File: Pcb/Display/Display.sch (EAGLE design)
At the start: 31 parts, among them J2 47219-2001, Q1 310mA/60V/1.6Ω

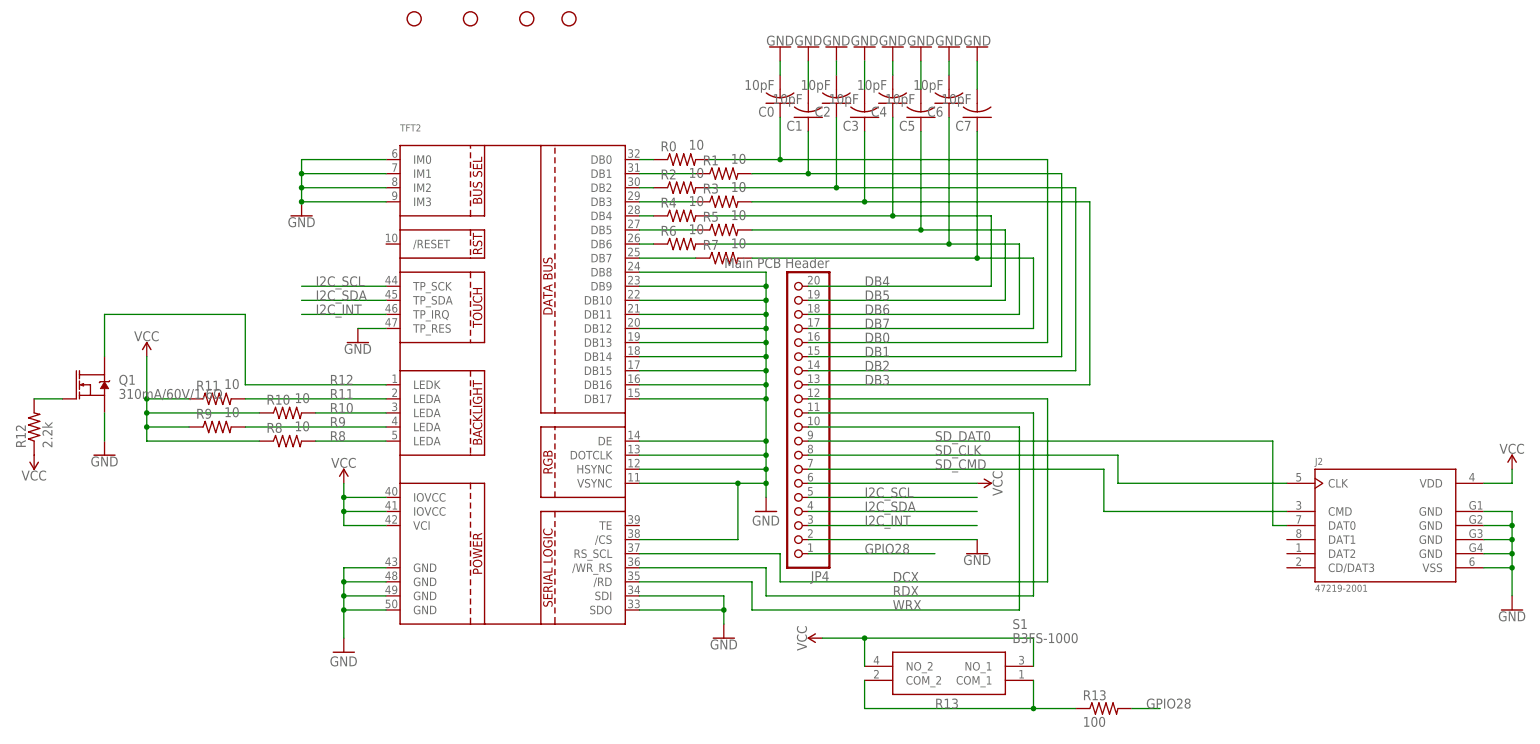
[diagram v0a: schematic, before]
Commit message: Updated PCB files and ported some of the graphics functions. The graphics changes are not tested yet.
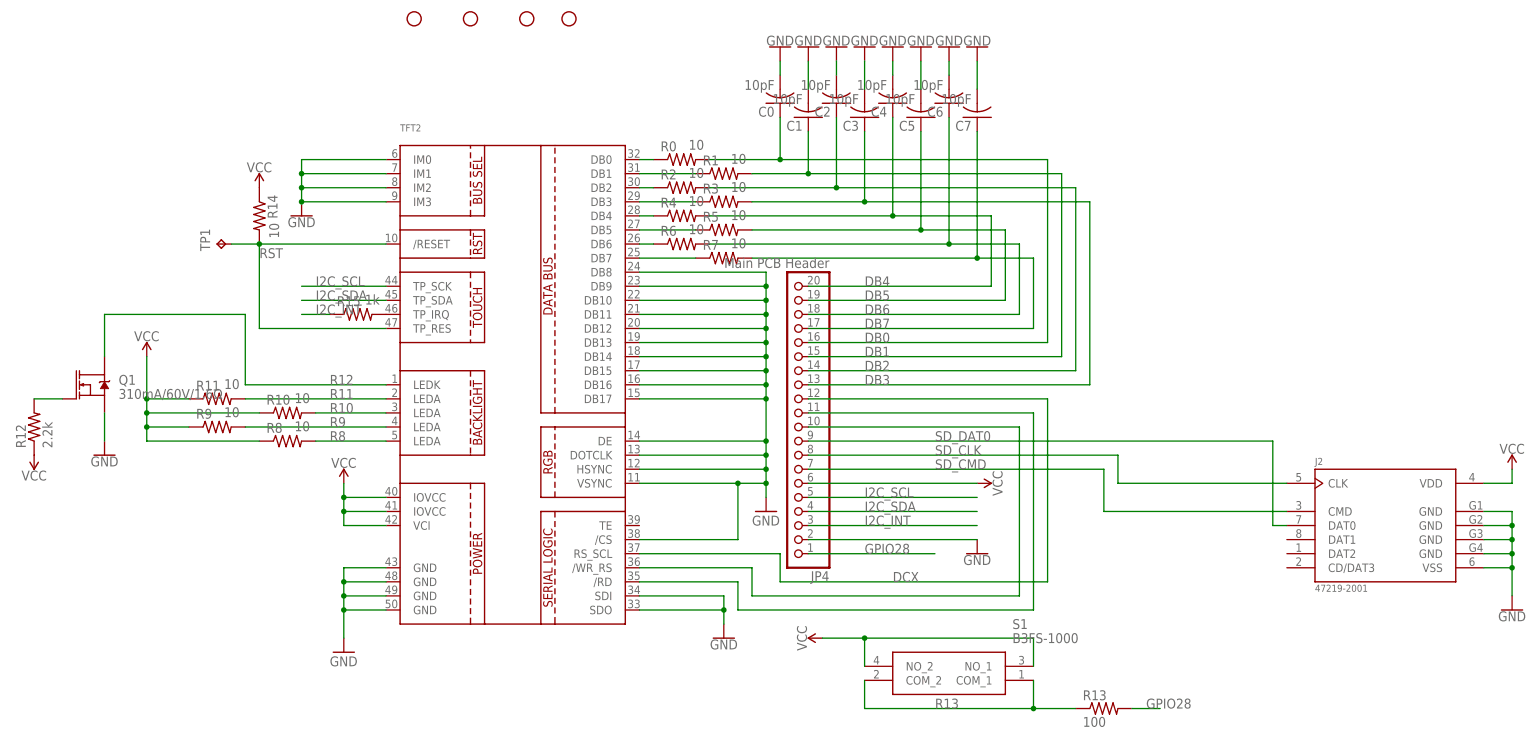
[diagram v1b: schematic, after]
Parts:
- added R14: 10, adafruit:R-US_R0805
- added R15: 1k, adafruit:R-US_R0805
- added TP1: TPTP09R, testpad:TPTP09R
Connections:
- new net N$4: R15.2, TFT2.TP_IRQ
- new net RST: R14.2, TFT2./RESET, TFT2.TP_RES, TP1.TP
- net GND: no longer TFT2.TP_RES
- net I2C_INT: now also R15.1; no longer TFT2.TP_IRQ
- net RDX: now also TFT2./RD; no longer TFT2./WR_RS
- net VCC: now also R14.1
- net WRX: now also TFT2./WR_RS; no longer TFT2./RD
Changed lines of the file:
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@@
 <?xml version="1.0" encoding="utf-8"?>
 <!DOCTYPE eagle SYSTEM "eagle.dtd">
-<eagle version="9.5.2">
+<eagle version="9.3.0">
 <drawing>
 <settings>
@@
 <part name="SUPPLY22" library="SparkFun-PowerSymbols" library_urn="urn:adsk.eagle:library:530" deviceset="VCC" device=""/>
 <part name="R12" library="rcl" library_urn="urn:adsk.eagle:library:334" deviceset="R-US_" device="M0805" package3d_urn="urn:adsk.eagle:package:23556/2" value="2.2k"/>
-<part name="GND40" library="SparkFun-PowerSymbols" library_urn="urn:adsk.eagle:library:530" deviceset="GND" device=""/>
 <part name="GND41" library="SparkFun-PowerSymbols" library_urn="urn:adsk.eagle:library:530" deviceset="GND" device=""/>
 <part name="R11" library="adafruit" deviceset="R-US_" device="R0805" value="10"/>
@@
 <part name="R6" library="adafruit" deviceset="R-US_" device="R0805" value="10"/>
 <part name="R7" library="adafruit" deviceset="R-US_" device="R0805" value="10"/>
+<part name="R14" library="adafruit" deviceset="R-US_" device="R0805" value="10"/>
+<part name="SUPPLY3" library="SparkFun-PowerSymbols" library_urn="urn:adsk.eagle:library:530" deviceset="VCC" device=""/>
+<part name="TP1" library="testpad" library_urn="urn:adsk.eagle:library:385" deviceset="TP" device="TP09R" package3d_urn="urn:adsk.eagle:package:27958/1"/>
+<part name="R15" library="adafruit" deviceset="R-US_" device="R0805" value="1k"/>
 </parts>
 <sheets>
@@
 <attribute name="VALUE" x="71.882" y="128.27" size="1.778" layer="96" rot="R90"/>
 </instance>
-<instance part="GND40" gate="1" x="127" y="147.32" smashed="yes">
-<attribute name="VALUE" x="127" y="147.066" size="1.778" layer="96" align="top-center"/>
-</instance>
 <instance part="GND41" gate="1" x="193.04" y="93.98" smashed="yes">
 <attribute name="VALUE" x="193.04" y="93.726" size="1.778" layer="96" align="top-center"/>
@@
 <attribute name="NAME" x="189.23" y="164.0586" size="1.778" layer="95"/>
 <attribute name="VALUE" x="194.31" y="164.338" size="1.778" layer="96"/>
+</instance>
+<instance part="R14" gate="G$1" x="109.22" y="170.18" smashed="yes" rot="R270">
+<attribute name="NAME" x="110.7186" y="173.99" size="1.778" layer="95" rot="R270"/>
+<attribute name="VALUE" x="110.998" y="168.91" size="1.778" layer="96" rot="R270"/>
+</instance>
+<instance part="SUPPLY3" gate="G$1" x="109.22" y="175.26" smashed="yes">
+<attribute name="VALUE" x="109.22" y="178.054" size="1.778" layer="96" align="bottom-center"/>
+</instance>
+<instance part="TP1" gate="G$1" x="101.6" y="165.1" smashed="yes" rot="R90">
+<attribute name="NAME" x="100.33" y="163.83" size="1.778" layer="95" rot="R90"/>
+<attribute name="TP_SIGNAL_NAME" x="102.87" y="166.37" size="1.778" layer="97" rot="R90"/>
+</instance>
+<instance part="R15" gate="G$1" x="127" y="152.4" smashed="yes">
+<attribute name="NAME" x="123.19" y="153.8986" size="1.778" layer="95"/>
+<attribute name="VALUE" x="128.27" y="154.178" size="1.778" layer="96"/>
 </instance>
 </instances>
@@
 </segment>
 <segment>
-<pinref part="TFT2" gate="G$1" pin="TP_RES"/>
-<wire x1="132.08" y1="149.86" x2="127" y2="149.86" width="0.1524" layer="91"/>
-<pinref part="GND40" gate="1" pin="GND"/>
-</segment>
-<segment>
 <pinref part="TFT2" gate="G$1" pin="SDI"/>
 <wire x1="177.8" y1="101.6" x2="193.04" y2="101.6" width="0.1524" layer="91"/>
@@
 <net name="I2C_INT" class="0">
 <segment>
-<pinref part="TFT2" gate="G$1" pin="TP_IRQ"/>
-<wire x1="132.08" y1="152.4" x2="116.84" y2="152.4" width="0.1524" layer="91"/>
-<label x="119.38" y="152.4" size="1.778" layer="95"/>
-</segment>
-<segment>
 <pinref part="JP4" gate="A" pin="3"/>
 <wire x1="208.28" y1="114.3" x2="238.76" y2="114.3" width="0.1524" layer="91"/>
 <label x="218.44" y="114.3" size="1.778" layer="95"/>
+</segment>
+<segment>
+<pinref part="R15" gate="G$1" pin="1"/>
+<wire x1="121.92" y1="152.4" x2="116.84" y2="152.4" width="0.1524" layer="91"/>
+<label x="119.38" y="152.4" size="1.778" layer="95"/>
 </segment>
 </net>
@@
 <pinref part="SUPPLY2" gate="G$1" pin="VCC"/>
 </segment>
+<segment>
+<pinref part="R14" gate="G$1" pin="1"/>
+<pinref part="SUPPLY3" gate="G$1" pin="VCC"/>
+</segment>
 </net>
 <net name="R11" class="0">
@@
 <net name="RDX" class="0">
 <segment>
+<wire x1="208.28" y1="134.62" x2="248.92" y2="134.62" width="0.1524" layer="91"/>
+<wire x1="248.92" y1="134.62" x2="248.92" y2="99.06" width="0.1524" layer="91"/>
+<pinref part="JP4" gate="A" pin="11"/>
+<wire x1="195.58" y1="99.06" x2="248.92" y2="99.06" width="0.1524" layer="91"/>
+<wire x1="195.58" y1="99.06" x2="195.58" y2="104.14" width="0.1524" layer="91"/>
+<pinref part="TFT2" gate="G$1" pin="/RD"/>
+<wire x1="195.58" y1="104.14" x2="177.8" y2="104.14" width="0.1524" layer="91"/>
+</segment>
+</net>
+<net name="WRX" class="0">
+<segment>
+<wire x1="198.12" y1="106.68" x2="198.12" y2="101.6" width="0.1524" layer="91"/>
+<wire x1="208.28" y1="132.08" x2="246.38" y2="132.08" width="0.1524" layer="91"/>
+<wire x1="246.38" y1="132.08" x2="246.38" y2="101.6" width="0.1524" layer="91"/>
+<pinref part="JP4" gate="A" pin="10"/>
+<wire x1="198.12" y1="101.6" x2="246.38" y2="101.6" width="0.1524" layer="91"/>
 <pinref part="TFT2" gate="G$1" pin="/WR_RS"/>
-<wire x1="177.8" y1="106.68" x2="200.66" y2="106.68" width="0.1524" layer="91"/>
-<wire x1="200.66" y1="106.68" x2="200.66" y2="101.6" width="0.1524" layer="91"/>
-<wire x1="208.28" y1="134.62" x2="248.92" y2="134.62" width="0.1524" layer="91"/>
-<wire x1="248.92" y1="134.62" x2="248.92" y2="101.6" width="0.1524" layer="91"/>
-<pinref part="JP4" gate="A" pin="11"/>
-<wire x1="200.66" y1="101.6" x2="248.92" y2="101.6" width="0.1524" layer="91"/>
-<label x="223.52" y="101.6" size="1.778" layer="95"/>
-</segment>
-</net>
-<net name="WRX" class="0">
-<segment>
-<pinref part="TFT2" gate="G$1" pin="/RD"/>
-<wire x1="177.8" y1="104.14" x2="198.12" y2="104.14" width="0.1524" layer="91"/>
-<wire x1="198.12" y1="104.14" x2="198.12" y2="99.06" width="0.1524" layer="91"/>
-<wire x1="208.28" y1="132.08" x2="246.38" y2="132.08" width="0.1524" layer="91"/>
-<wire x1="246.38" y1="132.08" x2="246.38" y2="99.06" width="0.1524" layer="91"/>
-<pinref part="JP4" gate="A" pin="10"/>
-<wire x1="198.12" y1="99.06" x2="246.38" y2="99.06" width="0.1524" layer="91"/>
-<label x="223.52" y="99.06" size="1.778" layer="95"/>
+<wire x1="198.12" y1="106.68" x2="177.8" y2="106.68" width="0.1524" layer="91"/>
 </segment>
 </net>
@@
 </segment>
 </net>
+<net name="RST" class="0">
+<segment>
+<pinref part="TFT2" gate="G$1" pin="/RESET"/>
+<wire x1="132.08" y1="165.1" x2="109.22" y2="165.1" width="0.1524" layer="91"/>
+<pinref part="R14" gate="G$1" pin="2"/>
+<wire x1="109.22" y1="165.1" x2="104.14" y2="165.1" width="0.1524" layer="91"/>
+<junction x="109.22" y="165.1"/>
+<pinref part="TP1" gate="G$1" pin="TP"/>
+<wire x1="109.22" y1="165.1" x2="109.22" y2="149.86" width="0.1524" layer="91"/>
+<pinref part="TFT2" gate="G$1" pin="TP_RES"/>
+<wire x1="109.22" y1="149.86" x2="132.08" y2="149.86" width="0.1524" layer="91"/>
+<label x="109.22" y="162.56" size="1.778" layer="95"/>
+</segment>
+</net>
+<net name="N$4" class="0">
+<segment>
+<pinref part="TFT2" gate="G$1" pin="TP_IRQ"/>
+<pinref part="R15" gate="G$1" pin="2"/>
+</segment>
+</net>
